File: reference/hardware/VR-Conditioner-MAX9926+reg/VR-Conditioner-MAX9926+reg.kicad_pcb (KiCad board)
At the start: 2 copper layers, 19.1 x 19.7 mm, 22 parts, among them J1 8-pin header, J2 Edge, U1 MAX9926UAEE+, U2 AMS1117CD-5.0

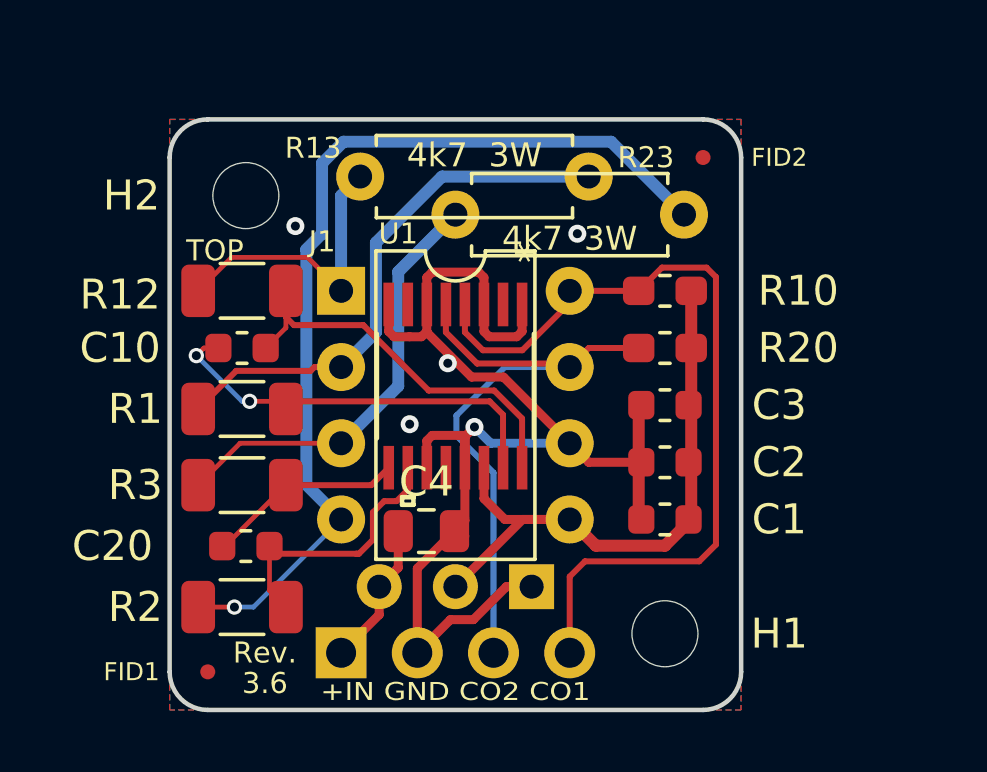
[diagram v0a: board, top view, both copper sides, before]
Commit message: Rev 3.7 give bigger resistors a bit more space. Add notes.
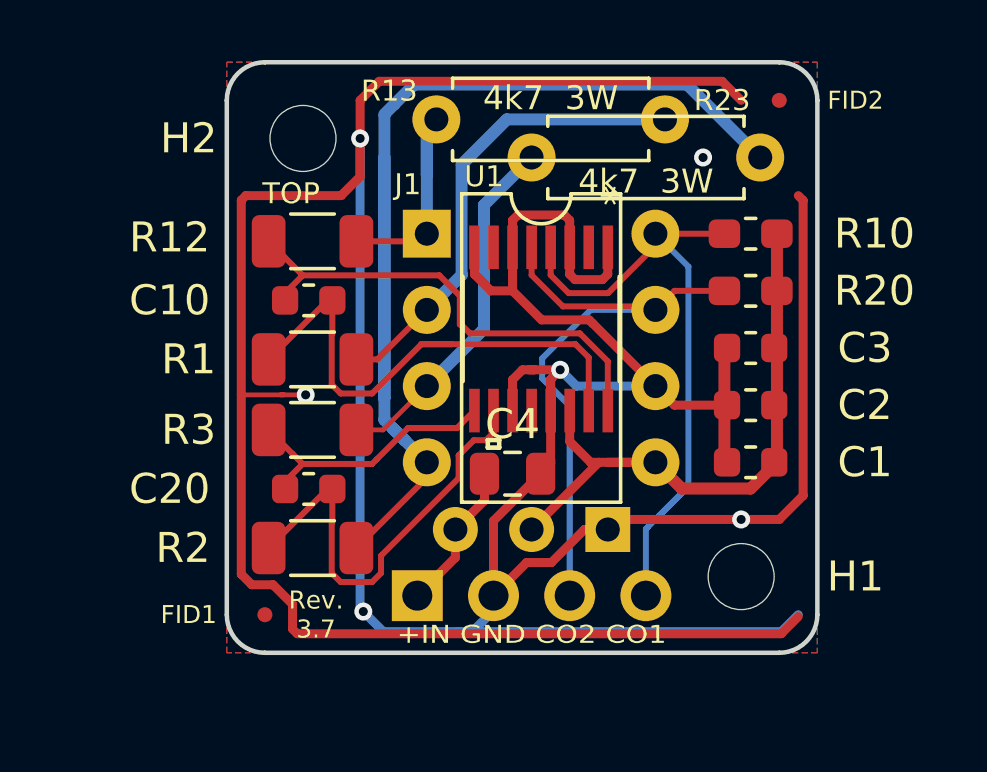
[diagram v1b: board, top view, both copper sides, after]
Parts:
- moved C4 3.45 mm to (121.9, 110.2)
- moved J1 3.43 mm to (119.1, 102.2)
- moved U1 3.43 mm to (122.9, 105.4)
- moved C1 3.43 mm to (129.9, 109.9)
- moved C2 3.43 mm to (129.9, 108.0)
- moved C3 3.43 mm to (129.9, 106.0)
- moved R10 3.43 mm to (129.9, 102.2)
- moved R20 3.43 mm to (129.9, 104.1)
- moved J2 3.18 mm to (118.7, 114.3)
- moved R23 3.18 mm to (122.6, 99.7)
- moved R13 3.17 mm to (119.4, 98.4)
- moved U2 3.17 mm to (125.1, 112.1)
- moved FID2 3.17 mm to (130.8, 97.8)
- moved H1 3.17 mm to (129.5, 113.7)
- moved R2 3.07 mm to (115.3, 112.7), turned to 0 degrees
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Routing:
- net GND: track 42.8 -> 148.7 mm, vias 5 -> 6
- net Net-(J1-Pad4): track 31.9 -> 38.5 mm, vias 1 -> 0
- net Net-(C20-Pad1): track 9.13 -> 14.9 mm
- net /COUT1: track 28.1 -> 22.7 mm
- net Net-(C10-Pad2): track 14.1 -> 18.1 mm, vias 2 -> 0
- net Net-(C10-Pad1): track 14.0 -> 17.0 mm
- net Net-(C20-Pad2): track 6.63 -> 9.65 mm
- net Net-(J1-Pad3): track 14.5 -> 12.0 mm
- net Net-(J1-Pad2): track 18.0 -> 15.8 mm
- net Net-(J1-Pad1): track 9.76 -> 7.60 mm
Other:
- board size 19.1 x 19.7 mm -> 19.7 x 19.7 mm
- board text added: "Rev. 3.7"
- board text added: "SoFar: + under 20x20mm & single sided for ‘Letter’ postage. + M2 mounting holes + Optional power resisotrs + Optional regulator for typical automotive power + Optional pin header for breadboard etc. + Could cut at pin header for direct PCB mount by castellation 2021424: Goal: Give left 6 passive components space from the left edge & the DIP Move signal trace away from right edge. Only traces by e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"
- board text removed: "3.6"
- board text removed: "Rev."
